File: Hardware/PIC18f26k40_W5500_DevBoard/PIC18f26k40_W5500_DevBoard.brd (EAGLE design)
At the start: 58.1 x 66.1 mm, 61 parts, among them J2 MAGJACK, J6 USB-B, U1 W5500, U2 PIC18F2523-I/SO, Y2 CRYSTAL-GROUNDEDSMD-3.2X2.5

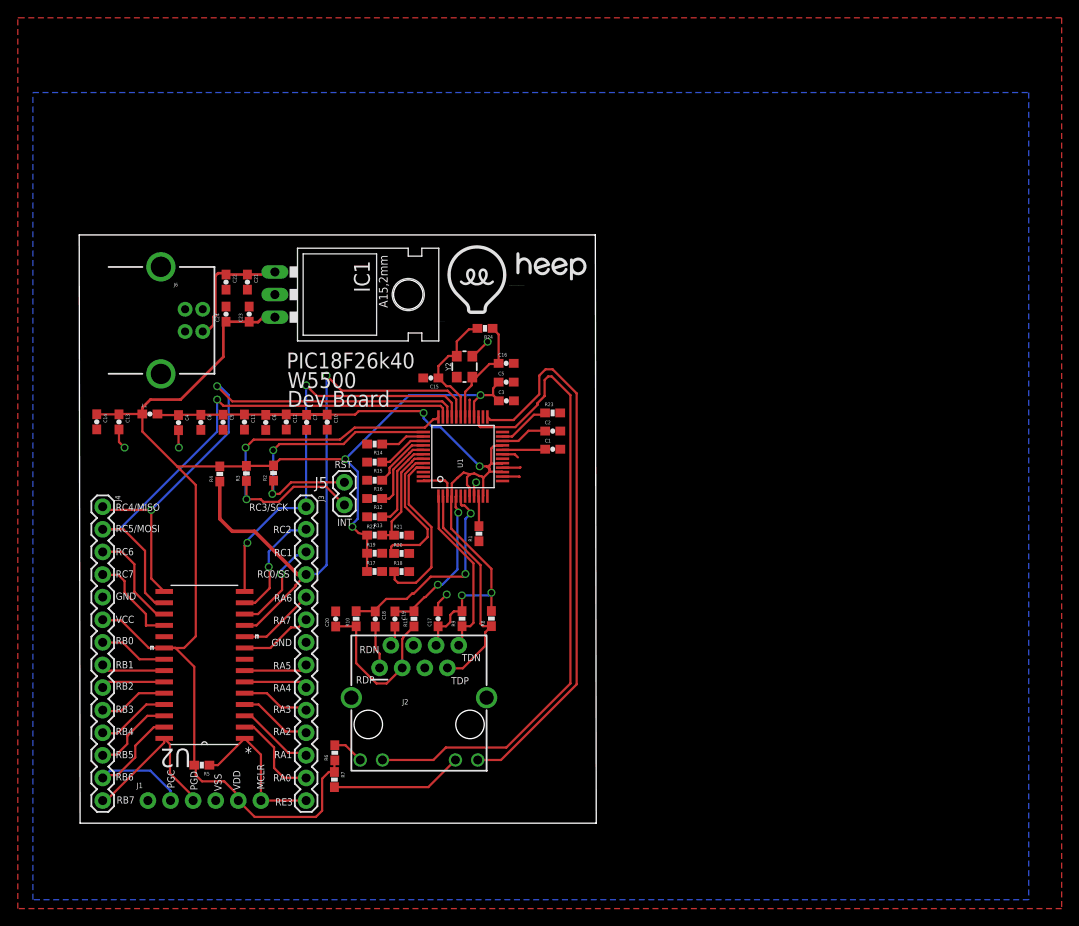
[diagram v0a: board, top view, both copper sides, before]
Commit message: #302 Added AC Playground to dev board
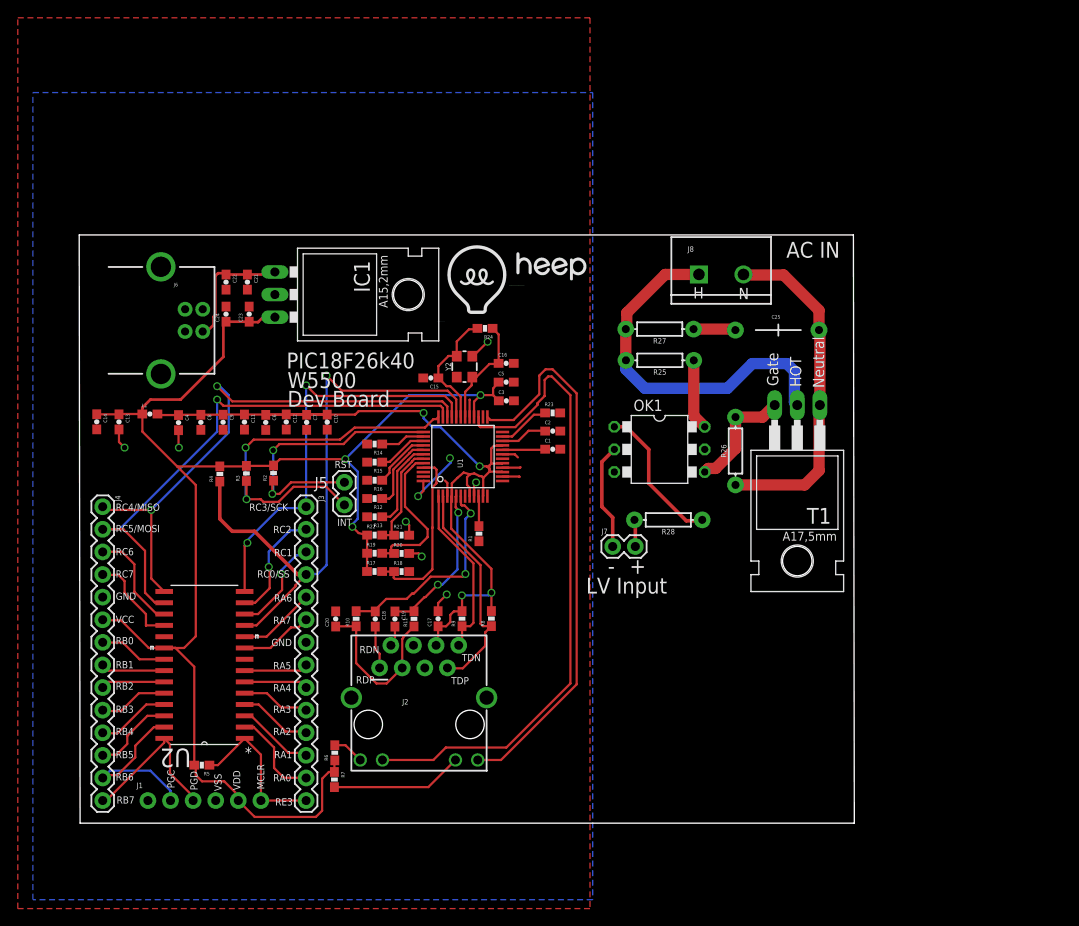
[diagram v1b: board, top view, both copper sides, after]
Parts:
- added C25: (no value), SparkFun-Capacitors:CAP-PTH-LARGE
- added J7: (no value), SparkFun-Connectors:1X02
- added J8: (no value), SparkFun-Connectors:SCREWTERMINAL-5MM-2
- added OK1: MOC3042T, optocoupler:DIL06B
- added R25, R26, R27, R28: 100k, SparkFun-Resistors:AXIAL-0.3
- added T1: BT138-H, triac:TO220BH
- J5: device SparkFun-Connectors:1X02 -> SparkFun-Connectors:1X02@1
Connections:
- new net CAPTORES: C25.1, R27.P$1
- new net GATE: OK1.4, R26.P$2, T1.G
- new net HOT: J8.1, R25.P$2, R27.P$2, T1.T2
- new net N$18: OK1.1, R28.P$1
- new net N$19: J7.1, OK1.2
- new net N$5: J7.2, R28.P$2
- new net NEUTRAL: C25.2, J8.2, R26.P$1, T1.T1
- new net RESTOMOC: OK1.6, R25.P$1
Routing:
- net HOT: track 0.00 -> 41.6 mm
- net NEUTRAL: track 0.00 -> 38.3 mm
- net N$18: track 0.00 -> 16.5 mm
- net GATE: track 0.00 -> 13.0 mm
- net N$19: track 0.00 -> 12.0 mm
- net GND: track 23.3 -> 32.0 mm, vias 5 -> 9
- net RESTOMOC: track 0.00 -> 7.98 mm
- net CAPTORES: track 0.00 -> 4.74 mm
- net N$5: track 0.00 -> 3.03 mm
- net PMODE1: track 16.1 -> 17.5 mm
- net PMODE0: track 19.3 -> 19.9 mm
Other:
- board size 58.1 x 66.1 mm -> 87.1 x 66.1 mm
- board text added: "+"
- board text added: "-"
- board text added: "AC IN"
- board text added: "Gate"
- board text added: "H"
- board text added: "HOT"
- board text added: "LV Input"
- board text added: "N"
- board text added: "Neutral"

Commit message: #302 Added play zone to AC Playground
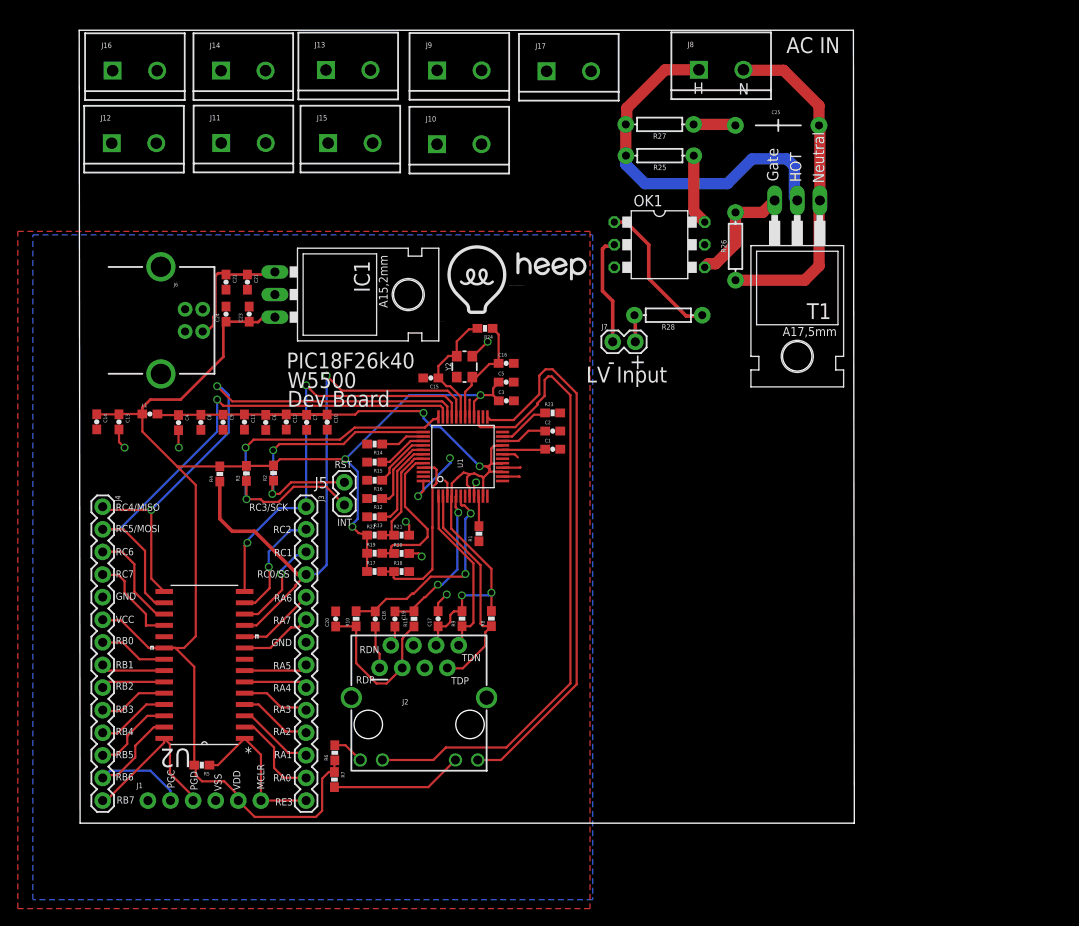
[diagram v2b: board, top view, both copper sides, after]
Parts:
- added J10, J11, J12, J13, J14, J15, J16, J17, J9: (no value), SparkFun-Connectors:SCREWTERMINAL-5MM-2
- moved R25 23.0 mm to (65.2, 75.0)
- moved J7 23.0 mm to (59.9, 54.1)
- moved C25 23.0 mm to (78.5, 78.4)
- moved J8 23.0 mm to (69.5, 84.7)
- moved OK1 23.0 mm to (65.1, 65.0)
- moved R28 23.0 mm to (66.1, 57.1)
- moved T1 23.0 mm to (80.6, 63.6)
- moved R26 23.0 mm to (73.7, 64.8)
- moved R27 23.0 mm to (65.1, 78.5)
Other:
- board size 87.1 x 66.1 mm -> 87.1 x 89.1 mm

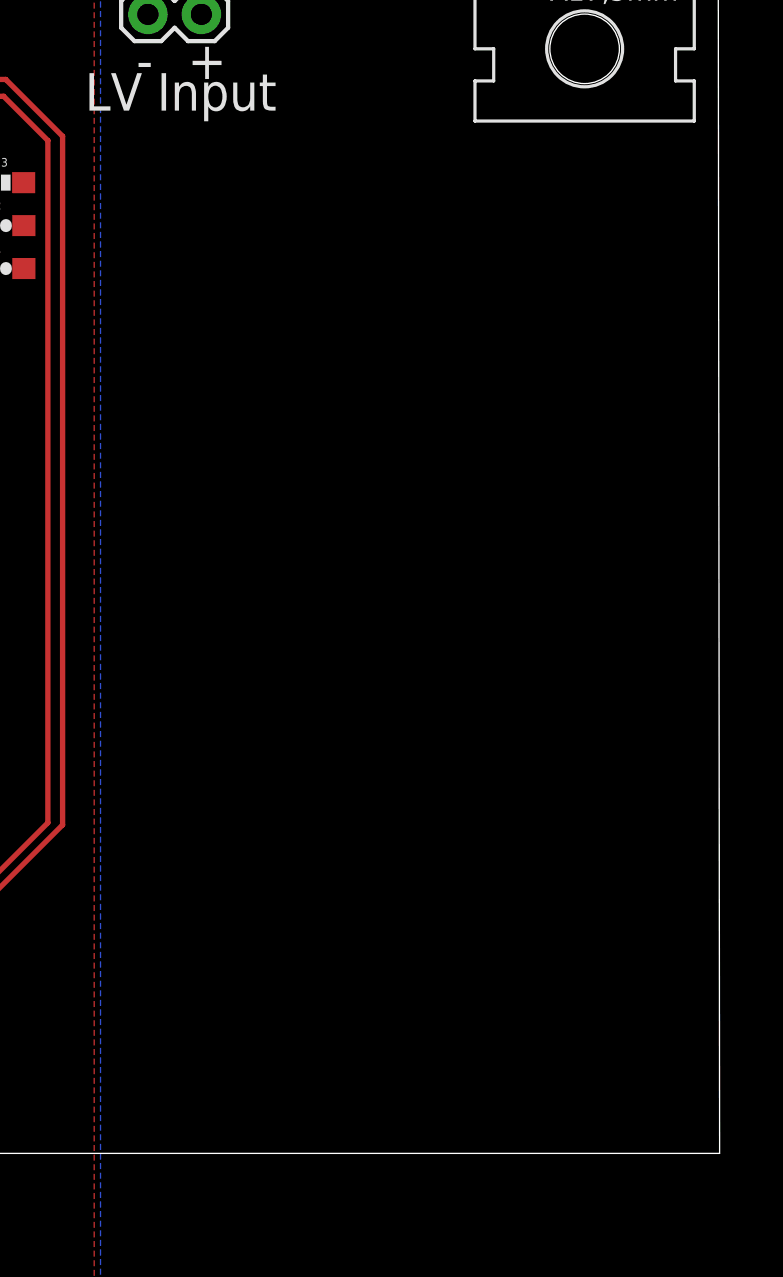
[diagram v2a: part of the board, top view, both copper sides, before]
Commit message: #302 Added a second AC Playgorund
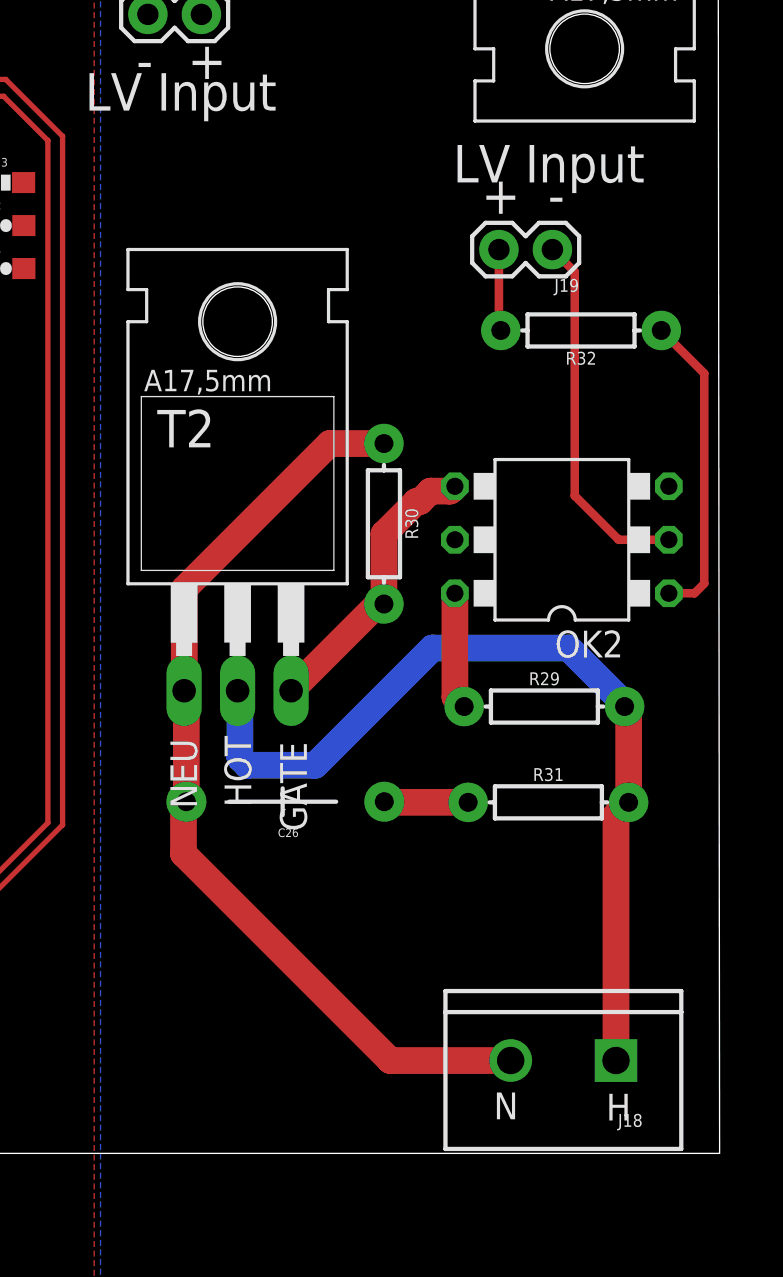
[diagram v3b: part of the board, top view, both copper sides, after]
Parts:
- added C26: (no value), SparkFun-Capacitors:CAP-PTH-LARGE
- added J18: (no value), SparkFun-Connectors:SCREWTERMINAL-5MM-2
- added J19: (no value), SparkFun-Connectors:1X02
- added OK2: MOC3042T, optocoupler:DIL06B
- added R29, R30, R31, R32: 100k, SparkFun-Resistors:AXIAL-0.3
- added T2: BT138-H, triac:TO220BH
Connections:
- new net CAPTORES2: C26.1, R31.P$1
- new net GATE2: OK2.4, R30.P$2, T2.G
- new net HOT2: J18.1, R29.P$2, R31.P$2, T2.T2
- new net N$20: J19.2, R32.P$2
- new net N$21: OK2.1, R32.P$1
- new net N$22: J19.1, OK2.2
- new net NEUTRAL2: C26.2, J18.2, R30.P$1, T2.T1
- new net RESTOMOC2: OK2.6, R29.P$1
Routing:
- net NEUTRAL2: track 0.00 -> 44.6 mm
- net HOT2: track 0.00 -> 42.3 mm
- net N$22: track 0.00 -> 17.5 mm
- net N$21: track 0.00 -> 14.7 mm
- net GATE2: track 0.00 -> 13.8 mm
- net RESTOMOC2: track 0.00 -> 5.56 mm
- net CAPTORES2: track 0.00 -> 4.00 mm
- net N$20: track 0.00 -> 3.88 mm
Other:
- board text added: "GATE"
- board text added: "NEU"
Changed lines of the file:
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@@
 <text x="68.9" y="81.96" size="1.27" layer="21">H</text>
 <text x="73.99" y="81.88" size="1.27" layer="21">N</text>
+<text x="74.34" y="46.11" size="1.778" layer="21">LV Input</text>
+<text x="75.69" y="44.62" size="1.778" layer="21">+</text>
+<text x="78.85" y="44.62" size="1.778" layer="21">-</text>
+<text x="81.61" y="1.56" size="1.27" layer="21">H</text>
+<text x="76.27" y="1.62" size="1.27" layer="21">N</text>
+<text x="67.4" y="15.3" size="1.27" layer="21" rot="R90">GATE</text>
+<text x="64.76" y="16.45" size="1.27" layer="21" rot="R90">HOT</text>
+<text x="62.19" y="16.38" size="1.27" layer="21" rot="R90">NEU</text>
 </plain>
 <attributes>
@@
 <attribute name="SF_SKU" value="PRT-08432" x="52.42" y="84.49" size="1.27" layer="27" display="off"/>
 </element>
+<element name="OK2" library="optocoupler" package="DIL06B" value="MOC3042T" x="79.51" y="29.14" rot="R90">
+<attribute name="MPN" value="" x="56.13" y="-11.01" size="1.27" layer="27" rot="R90" display="off"/>
+<attribute name="MF" value="" x="56.13" y="-11.01" size="1.27" layer="27" rot="R90" display="off"/>
+<attribute name="OC_FARNELL" value="unknown" x="56.13" y="-11.01" size="1.27" layer="27" rot="R90" display="off"/>
+<attribute name="OC_NEWARK" value="unknown" x="56.13" y="-11.01" size="1.27" layer="27" rot="R90" display="off"/>
+</element>
+<element name="J18" library="SparkFun-Connectors" package="SCREWTERMINAL-5MM-2" value="" x="82.08" y="4.41" rot="R180">
+<attribute name="SF_SKU" value="PRT-08432" x="140.52" y="4.41" size="1.27" layer="27" rot="R180" display="off"/>
+</element>
+<element name="R29" library="SparkFun-Resistors" package="AXIAL-0.3" value="100k" x="78.68" y="21.22">
+<attribute name="PROD_ID" value="RES-12184" x="31.93" y="31" size="1.27" layer="27" display="off"/>
+</element>
+<element name="R30" library="SparkFun-Resistors" package="AXIAL-0.3" value="100k" x="71.06" y="29.9" rot="R270">
+<attribute name="PROD_ID" value="RES-12184" x="81.1" y="48.2" size="1.27" layer="27" rot="R270" display="off"/>
+</element>
+<element name="T2" library="triac" package="TO220BH" value="BT138-H" x="64.11" y="28.32"/>
+<element name="C26" library="SparkFun-Capacitors" package="CAP-PTH-LARGE" value="" x="66.25" y="16.7" rot="R180"/>
+<element name="R31" library="SparkFun-Resistors" package="AXIAL-0.3" value="100k" x="78.87" y="16.67">
+<attribute name="PROD_ID" value="RES-12184" x="12.3" y="-11.15" size="1.27" layer="27" display="off"/>
+</element>
+<element name="R32" library="SparkFun-Resistors" package="AXIAL-0.3" value="100k" x="80.42" y="39.08" rot="R180">
+<attribute name="PROD_ID" value="RES-12184" x="120.57" y="66.9" size="1.27" layer="27" rot="R180" display="off"/>
+</element>
+<element name="J19" library="SparkFun-Connectors" package="1X02" value="" x="79.06" y="42.92" rot="R180"/>
 </elements>
 <signals>
@@
 <wire x1="73.524" y1="78.52" x2="73.634" y2="78.41" width="1.27" layer="1"/>
 </signal>
+<signal name="N$20">
+<contactref element="J19" pad="2"/>
+<contactref element="R32" pad="P$2"/>
+<wire x1="76.52" y1="42.92" x2="76.52" y2="39.17" width="0.4064" layer="1"/>
+<wire x1="76.52" y1="39.17" x2="76.61" y2="39.08" width="0.4064" layer="1"/>
+</signal>
+<signal name="N$21">
+<contactref element="R32" pad="P$1"/>
+<contactref element="OK2" pad="1"/>
+<wire x1="84.59" y1="26.6" x2="85.81" y2="26.6" width="0.4064" layer="1"/>
+<wire x1="85.81" y1="26.6" x2="86.27" y2="27.06" width="0.4064" layer="1"/>
+<wire x1="86.27" y1="27.06" x2="86.27" y2="37.04" width="0.4064" layer="1"/>
+<wire x1="86.27" y1="37.04" x2="84.23" y2="39.08" width="0.4064" layer="1"/>
+</signal>
+<signal name="N$22">
+<contactref element="OK2" pad="2"/>
+<contactref element="J19" pad="1"/>
+<wire x1="84.59" y1="29.14" x2="82.21" y2="29.14" width="0.4064" layer="1"/>
+<wire x1="82.21" y1="29.14" x2="80.12" y2="31.23" width="0.4064" layer="1"/>
+<wire x1="80.12" y1="31.23" x2="80.12" y2="41.86" width="0.4064" layer="1"/>
+<wire x1="80.12" y1="41.86" x2="79.06" y2="42.92" width="0.4064" layer="1"/>
+</signal>
+<signal name="RESTOMOC2">
+<contactref element="R29" pad="P$1"/>
+<contactref element="OK2" pad="6"/>
+<wire x1="74.43" y1="26.6" x2="74.43" y2="21.66" width="1.27" layer="1"/>
+<wire x1="74.43" y1="21.66" x2="74.87" y2="21.22" width="1.27" layer="1"/>
+</signal>
+<signal name="GATE2">
+<contactref element="OK2" pad="4"/>
+<contactref element="T2" pad="G"/>
+<contactref element="R30" pad="P$2"/>
+<wire x1="71.06" y1="29.42" x2="71.06" y2="26.09" width="1.27" layer="1"/>
+<wire x1="71.06" y1="29.42" x2="72.6" y2="30.96" width="1.27" layer="1"/>
+<wire x1="72.6" y1="30.96" x2="72.78" y2="30.96" width="1.27" layer="1"/>
+<wire x1="72.78" y1="30.96" x2="73.27" y2="31.45" width="1.27" layer="1"/>
+<wire x1="73.27" y1="31.45" x2="74.2" y2="31.45" width="1.27" layer="1"/>
+<wire x1="74.2" y1="31.45" x2="74.43" y2="31.68" width="1.27" layer="1"/>
+<wire x1="71.06" y1="26.09" x2="70.77" y2="26.09" width="1.27" layer="1"/>
+<wire x1="70.77" y1="26.09" x2="66.65" y2="21.97" width="1.27" layer="1"/>
+</signal>
+<signal name="HOT2">
+<contactref element="T2" pad="T2"/>
+<contactref element="R29" pad="P$2"/>
+<contactref element="J18" pad="1"/>
+<contactref element="R31" pad="P$2"/>
+<wire x1="82.68" y1="16.67" x2="82.68" y2="21.03" width="1.27" layer="1"/>
+<wire x1="82.68" y1="21.03" x2="82.49" y2="21.22" width="1.27" layer="1"/>
+<wire x1="82.08" y1="4.41" x2="82.08" y2="16.07" width="1.27" layer="1"/>
+<wire x1="82.08" y1="16.07" x2="82.68" y2="16.67" width="1.27" layer="1"/>
+<wire x1="82.49" y1="21.22" x2="82.49" y2="21.34" width="1.27" layer="16"/>
+<wire x1="82.49" y1="21.34" x2="79.83" y2="24" width="1.27" layer="16"/>
+<wire x1="79.83" y1="24" x2="73.36" y2="24" width="1.27" layer="16"/>
+<wire x1="73.36" y1="24" x2="67.79" y2="18.43" width="1.27" layer="16"/>
+<wire x1="67.79" y1="18.43" x2="64.57" y2="18.43" width="1.27" layer="16"/>
+<wire x1="64.57" y1="18.43" x2="64.22" y2="18.78" width="1.27" layer="16"/>
+<wire x1="64.22" y1="18.78" x2="64.22" y2="21.86" width="1.27" layer="16"/>
+<wire x1="64.22" y1="21.86" x2="64.11" y2="21.97" width="1.27" layer="16"/>
+</signal>
+<signal name="CAPTORES2">
+<contactref element="C26" pad="1"/>
+<contactref element="R31" pad="P$1"/>
+<wire x1="75.06" y1="16.67" x2="71.106" y2="16.67" width="1.27" layer="1"/>
+<wire x1="71.106" y1="16.67" x2="71.076" y2="16.7" width="1.27" layer="1"/>
+</signal>
+<signal name="NEUTRAL2">
+<contactref element="J18" pad="2"/>
+<contactref element="R30" pad="P$1"/>
+<contactref element="T2" pad="T1"/>
+<contactref element="C26" pad="2"/>
+<wire x1="77.08" y1="4.41" x2="71.36" y2="4.41" width="1.27" layer="1"/>
+<wire x1="71.36" y1="4.41" x2="61.54" y2="14.23" width="1.27" layer="1"/>
+<wire x1="61.54" y1="14.23" x2="61.54" y2="16.562" width="1.27" layer="1"/>
+<wire x1="61.54" y1="16.562" x2="61.678" y2="16.7" width="1.27" layer="1"/>
+<wire x1="61.678" y1="16.7" x2="61.678" y2="21.862" width="1.27" layer="1"/>
+<wire x1="61.57" y1="21.97" x2="61.678" y2="21.862" width="1.27" layer="1"/>
+<wire x1="71.06" y1="33.71" x2="68.48" y2="33.71" width="1.27" layer="1"/>
+<wire x1="68.48" y1="33.71" x2="61.58" y2="26.81" width="1.27" layer="1"/>
+<wire x1="61.58" y1="26.81" x2="61.58" y2="21.98" width="1.27" layer="1"/>
+<wire x1="61.58" y1="21.98" x2="61.57" y2="21.97" width="1.27" layer="1"/>
+</signal>
 </signals>
